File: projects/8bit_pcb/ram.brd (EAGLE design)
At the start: 100 x 80 mm, 100 parts, among them IC1 74LS00N

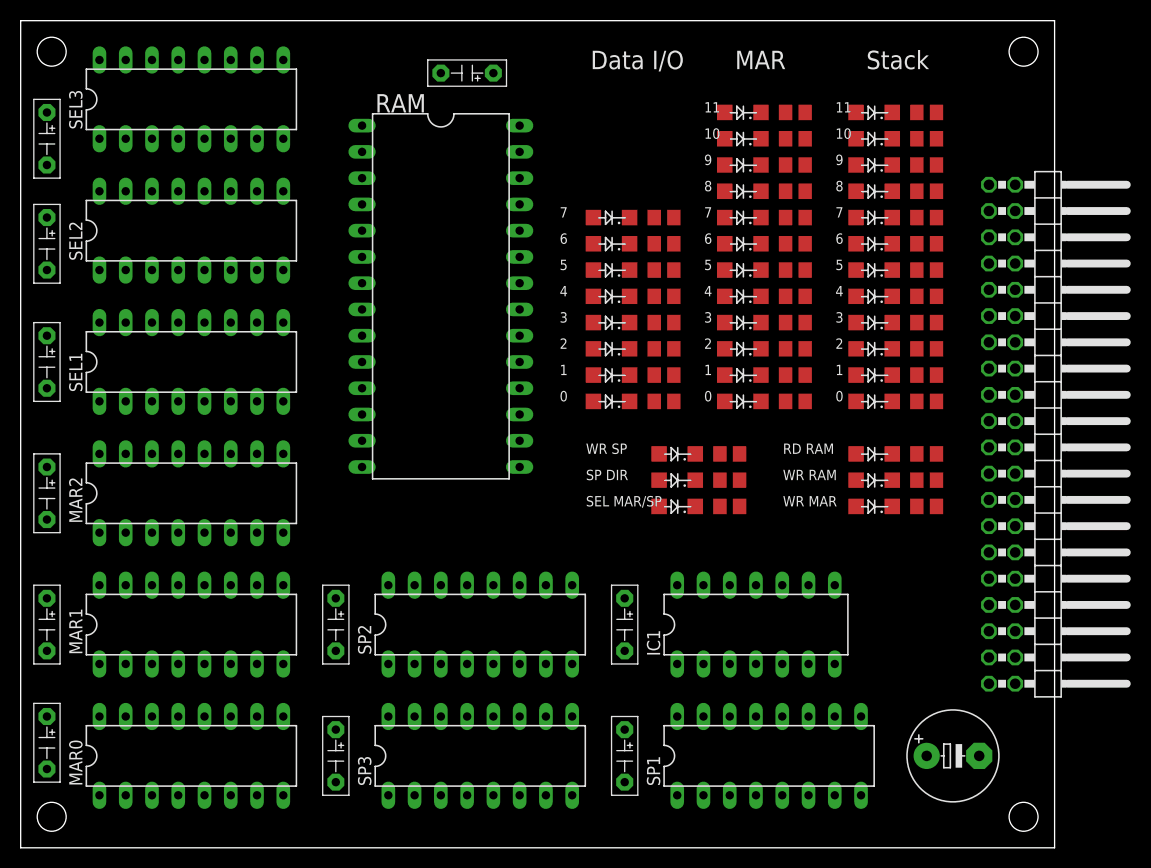
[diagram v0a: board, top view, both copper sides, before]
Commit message: RAM, Disp16Seg, Decoder
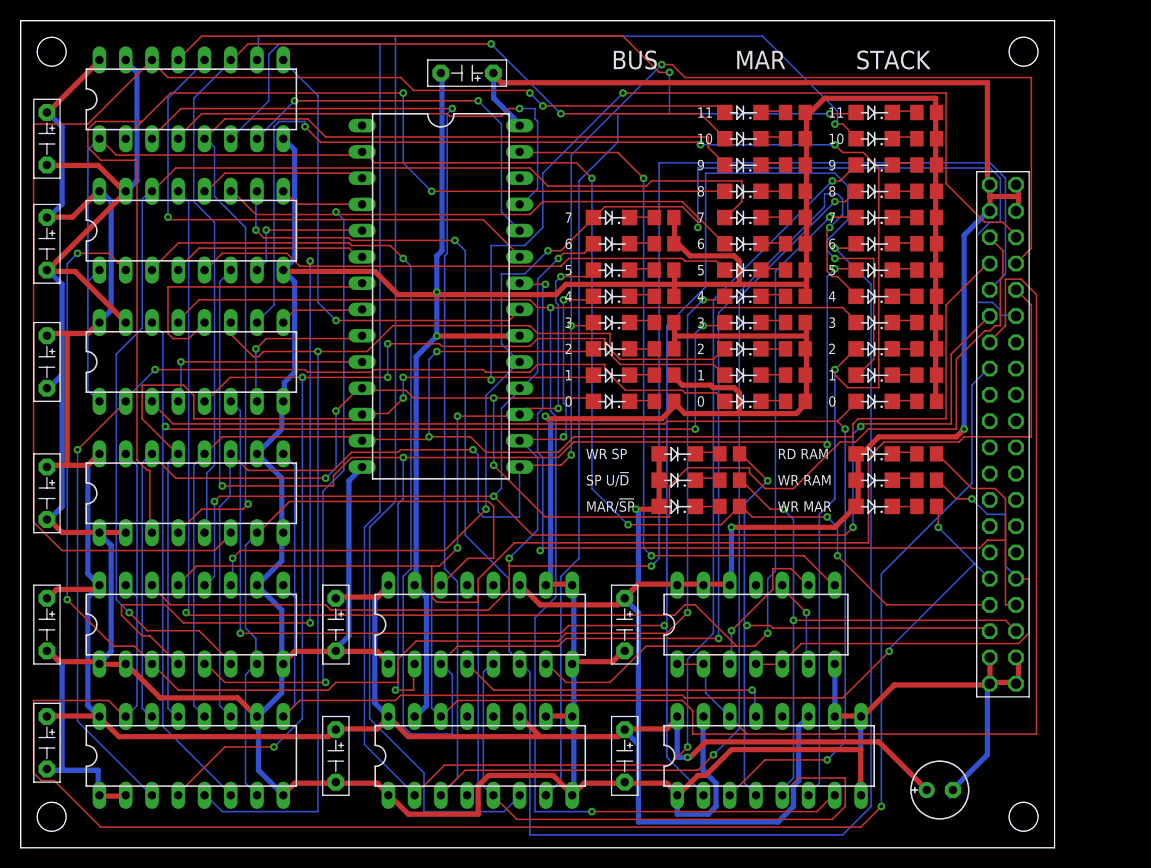
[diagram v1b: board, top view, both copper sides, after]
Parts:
- removed C1: 10u, rcl:E5-8,5
- removed JP1: (no value), pinhead:2X20/90
- added C8: 10n, rcl:E2,5-6E
- added U$12: 2X40, IsaacAlonso:2X40
- RAM: value (none) -> 28C64
- moved LED13 27.9 mm to (82.5, 43.2)
- moved LED32 27.9 mm to (82.5, 71.1)
- moved R13 27.9 mm to (87.6, 43.2)
- moved R32 27.9 mm to (87.6, 71.1)
- moved LED14 22.9 mm to (82.5, 45.7)
- moved LED31 22.9 mm to (82.5, 68.6)
- moved R14 22.9 mm to (87.6, 45.7)
- moved R31 22.9 mm to (87.6, 68.6)
- moved LED15 17.8 mm to (82.5, 48.3)
- moved LED30 17.8 mm to (82.5, 66.0)
- moved R15 17.8 mm to (87.6, 48.3)
- moved R30 17.8 mm to (87.6, 66.0)
- moved LED16 12.7 mm to (82.5, 50.8)
- moved LED29 12.7 mm to (82.5, 63.5)
- moved R16 12.7 mm to (87.6, 50.8)
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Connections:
- removed net !RD_MAR: JP1.30
- removed net !RD_SP: JP1.32
- removed net ADDR12: JP1.25, RAM.2
- removed net DATA0: LED17.A
- removed net DATA1: LED18.A
- removed net DATA2: LED19.A
- removed net DATA3: LED20.A
- removed net DATA4: LED21.A
- removed net DATA5: LED22.A
- removed net DATA6: LED23.A
- removed net DATA7: LED24.A
- removed net DATA_DIR: JP1.21
- removed net DATA_EN: JP1.23
- removed net ICLK: JP1.14
- net !RD_RAM: now also U$12.P23; no longer JP1.34
- net !WR_MAR: now also U$12.P15; no longer JP1.29
- net !WR_RAM: now also U$12.P24; no longer JP1.33
- net !WR_SP: now also U$12.P17; no longer JP1.31
- net BUS0: now also LED17.A, U$12.P2; no longer JP1.5
- net BUS1: now also LED18.A, U$12.P37; no longer JP1.6
- net BUS2: now also LED19.A, U$12.P3; no longer JP1.7
- net BUS3: now also LED20.A, U$12.P36; no longer JP1.8
- net BUS4: now also LED21.A, U$12.P4; no longer JP1.9
- net BUS5: now also LED22.A, U$12.P35; no longer JP1.10
- net BUS6: now also LED23.A, U$12.P5; no longer JP1.11
- net BUS7: now also LED24.A, U$12.P34; no longer JP1.12
- net CLK: now also U$12.P6; no longer JP1.13
- net GND: now also C8.-, U$1.P-, U$10.P-, U$11.P-, U$12.P18, U$12.P19, U$12.P20, U$12.P21, U$2.P-, U$3.P-, U$4.P-, U$5.P-, U$6.P-, U$7.P-, U$8.P-, U$9.P-; no longer C1.-, JP1.37, JP1.38, JP1.39, JP1.40
- net RST: now also U$12.P7; no longer JP1.15
- net SEL_MAR/SP: now also RAM.2, U$12.P16; no longer JP1.20
- net SP_DIR: now also U$12.P22; no longer JP1.18
- net VCC: now also C8.+, IC1.12, IC1.13, U$1.P+, U$10.P+, U$11.P+, U$12.P0, U$12.P1, U$12.P38, U$12.P39, U$2.P+, U$3.P+, U$4.P+, U$5.P+, U$6.P+, U$7.P+, U$8.P+, U$9.P+; no longer C1.+, JP1.1, JP1.2, JP1.3, JP1.4
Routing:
- net GND: track 0.00 -> 681.5 mm, vias 0 -> 3
- net VCC: track 0.00 -> 430.8 mm, vias 0 -> 4
- net CLK: track 0.00 -> 201.2 mm
- net SP9: track 0.00 -> 188.0 mm, vias 0 -> 2
- net SP8: track 0.00 -> 187.1 mm, vias 0 -> 3
- net RST: track 0.00 -> 176.2 mm, vias 0 -> 1
- net SP6: track 0.00 -> 176.0 mm, vias 0 -> 3
- net SP4: track 0.00 -> 173.0 mm, vias 0 -> 3
- net BUS4: track 0.00 -> 172.1 mm, vias 0 -> 4
- net BUS3: track 0.00 -> 170.4 mm, vias 0 -> 4
- net BUS1: track 0.00 -> 168.0 mm, vias 0 -> 4
- net SP7: track 0.00 -> 166.1 mm, vias 0 -> 3
- net SP1: track 0.00 -> 165.8 mm, vias 0 -> 3
- net BUS0: track 0.00 -> 159.5 mm, vias 0 -> 4
- net BUS5: track 0.00 -> 156.7 mm, vias 0 -> 4
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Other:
- board text added: "BUS"
- board text added: "MAR/!SP"
- board text added: "SP U/!D"
- board text added: "STACK"
- board text removed: "Data I/O"
- board text removed: "SEL MAR/SP"
- board text removed: "SP DIR"
- board text removed: "Stack"
